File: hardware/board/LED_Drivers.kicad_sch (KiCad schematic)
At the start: 69 parts

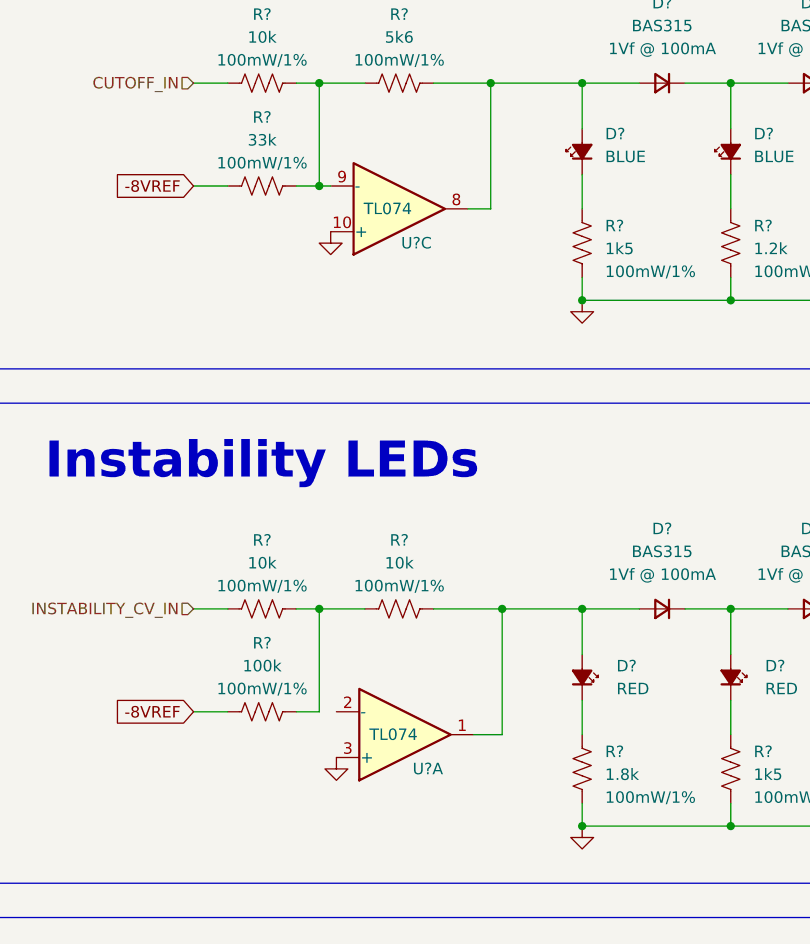
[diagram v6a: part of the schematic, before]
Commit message: First Draft of layout V2 (All components facing the same way)
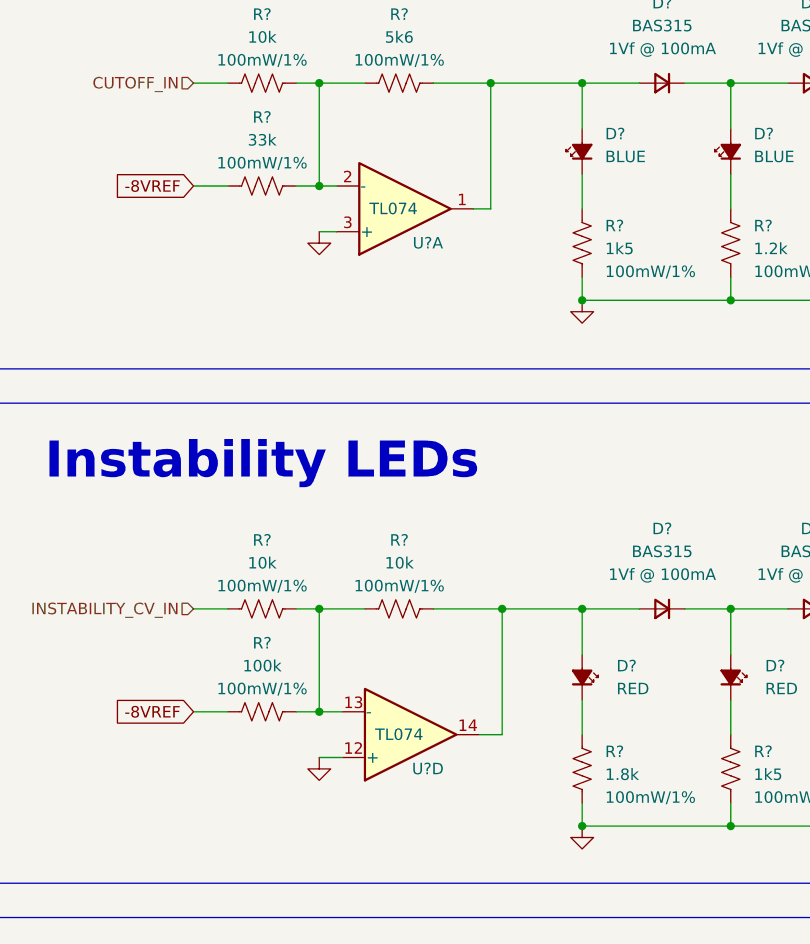
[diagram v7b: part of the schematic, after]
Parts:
- removed U?: TL074, Package_SO:TSSOP-14_4.4x5mm_P0.65mm, symbol winterbloom:TL074
- added U?: TL074, Package_SO:TSSOP-14_4.4x5mm_P0.65mm, symbol winterbloom:TL074
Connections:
- net GND: now also U?.12 (+)
- net at D?.2 (A), D?.2 (A), R?.1: now also U?.1
- net at R?.1, R?.1, R?.2: now also U?.2 (-)
- net at R?.1, R?.1, R?.2: now also U?.13 (-)
- net at D?.2 (A), D?.2 (A), R?.1: now also U?.14; no longer U?.1
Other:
- moved on the sheet: U?A
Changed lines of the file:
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@@
   (junction (at 208.28 119.38) (diameter 0) (color 0 0 0 0)
   )
+  (junction (at 55.88 64.77) (diameter 0) (color 0 0 0 0)
+  )
   (junction (at 205.74 53.34) (diameter 0) (color 0 0 0 0)
   )
@@
   (junction (at 85.09 77.47) (diameter 0) (color 0 0 0 0)
   )
+  (junction (at 55.88 123.19) (diameter 0) (color 0 0 0 0)
+  )
   (junction (at 55.88 167.64) (diameter 0) (color 0 0 0 0)
   )
-  (junction (at 55.88 64.77) (diameter 0) (color 0 0 0 0)
-  )
   (junction (at 224.79 153.67) (diameter 0) (color 0 0 0 0)
   )
@@
     (stroke (width 0) (type default))
   )
+  (wire (pts (xy 55.88 128.27) (xy 58.42 128.27))
+    (stroke (width 0) (type default))
+  )
   (wire (pts (xy 85.09 74.93) (xy 85.09 77.47))
     (stroke (width 0) (type default))
@@
     (stroke (width 0) (type default))
   )
+  (wire (pts (xy 73.025 67.31) (xy 74.93 67.31))
+    (stroke (width 0) (type default))
+  )
   (wire (pts (xy 173.99 64.77) (xy 176.53 64.77))
     (stroke (width 0) (type default))
@@
     (stroke (width 0) (type default))
   )
+  (wire (pts (xy 55.88 123.19) (xy 58.42 123.19))
+    (stroke (width 0) (type default))
+  )
   (wire (pts (xy 200.66 119.38) (xy 208.28 119.38))
     (stroke (width 0) (type default))
@@
     (stroke (width 0) (type default))
   )
-  (wire (pts (xy 57.15 64.77) (xy 55.88 64.77))
-    (stroke (width 0) (type default))
-  )
   (wire (pts (xy 85.09 167.64) (xy 85.09 172.72))
     (stroke (width 0) (type default))
@@
     (stroke (width 0) (type default))
   )
-  (wire (pts (xy 73.025 125.73) (xy 76.2 125.73))
-    (stroke (width 0) (type default))
-  )
   (wire (pts (xy 85.09 189.23) (xy 85.09 194.31))
     (stroke (width 0) (type default))
@@
     (stroke (width 0) (type default))
   )
+  (wire (pts (xy 73.66 125.73) (xy 76.2 125.73))
+    (stroke (width 0) (type default))
+  )
   (wire (pts (xy 205.74 53.34) (xy 205.74 58.42))
     (stroke (width 0) (type default))
@@
     (stroke (width 0) (type default))
   )
+  (wire (pts (xy 55.88 64.77) (xy 57.785 64.77))
+    (stroke (width 0) (type default))
+  )
   (wire (pts (xy 208.28 133.35) (xy 219.71 133.35))
     (stroke (width 0) (type default))
@@
     (stroke (width 0) (type default))
   )
+  (wire (pts (xy 55.88 69.85) (xy 57.785 69.85))
+    (stroke (width 0) (type default))
+  )
   (wire (pts (xy 224.79 119.38) (xy 228.6 119.38))
     (stroke (width 0) (type default))
@@
   )
   (wire (pts (xy 76.2 167.64) (xy 76.2 181.61))
-    (stroke (width 0) (type default))
-  )
-  (wire (pts (xy 72.39 67.31) (xy 74.93 67.31))
     (stroke (width 0) (type default))
   )
@@
     )
   )
-  (symbol (lib_id "winterbloom:TL074") (at 64.77 67.31 0) (mirror x) (unit 3)
-    (in_bom yes) (on_board yes) (dnp no)
-    (property "Reference" "U?" (at 66.675 71.12 0)
-      (effects (font (size 1.27 1.27)))
-    )
-    (property "Value" "TL074" (at 63.5 67.31 0)
-      (effects (font (size 1.27 1.27)))
-    )
-    (property "Footprint" "Package_SO:TSSOP-14_4.4x5mm_P0.65mm" (at 64.77 77.47 0)
-      (effects (font (size 1.27 1.27)) hide)
-    )
-    (property "Datasheet" "https://www.ti.com/lit/ds/symlink/tl071.pdf" (at 66.04 72.39 0)
-      (effects (font (size 1.27 1.27)) hide)
-    )
-    (property "MPN" "TL074CPW" (at 64.77 74.93 0)
+  (symbol (lib_id "winterbloom:TL074") (at 66.04 125.73 0) (mirror x) (unit 4)
+    (in_bom yes) (on_board yes) (dnp no)
+    (property "Reference" "U?" (at 67.945 129.54 0)
+      (effects (font (size 1.27 1.27)))
+    )
+    (property "Value" "TL074" (at 64.77 125.73 0)
+      (effects (font (size 1.27 1.27)))
+    )
+    (property "Footprint" "Package_SO:TSSOP-14_4.4x5mm_P0.65mm" (at 66.04 135.89 0)
+      (effects (font (size 1.27 1.27)) hide)
+    )
+    (property "Datasheet" "https://www.ti.com/lit/ds/symlink/tl071.pdf" (at 67.31 130.81 0)
+      (effects (font (size 1.27 1.27)) hide)
+    )
+    (property "MPN" "TL074CPW" (at 66.04 133.35 0)
       (effects (font (size 1.27 1.27)) hide)
     )
@@
     (pin "4")
     (instances
-      (project "VCA_0.3"
-        (path "/0739a502-7fa1-4e85-8cae-604fd21c9156"
-          (reference "U?") (unit 3)
-        )
-      )
       (project "mainboard"
         (path "/6e47ee4f-b36d-4cb2-9b20-31f755e664f7/00000000-0000-0000-0000-00005f0e55e2"
-          (reference "U?") (unit 3)
+          (reference "U?") (unit 4)
         )
         (path "/6e47ee4f-b36d-4cb2-9b20-31f755e664f7/00000000-0000-0000-0000-00005f016ad7"
-          (reference "U?") (unit 2)
-        )
-      )
-      (project "mainboard"
-        (path "/960bd036-bf0c-45ea-9f41-1321756e0e5a/2fb572ad-24ea-4cbe-ad52-b6fc76c2d017"
-          (reference "U?") (unit 3)
-        )
-        (path "/960bd036-bf0c-45ea-9f41-1321756e0e5a"
-          (reference "U?") (unit 3)
-        )
-        (path "/960bd036-bf0c-45ea-9f41-1321756e0e5a/48d891c0-35ba-4c8e-a930-c990a10298eb"
-          (reference "U4") (unit 3)
-        )
-        (path "/960bd036-bf0c-45ea-9f41-1321756e0e5a/e3d5295b-e037-4c01-a5ad-25ec0ca0bdb3"
-          (reference "U4") (unit 3)
-        )
-      )
-      (project "VCA"
-        (path "/de69ad6f-07bb-4f9c-962b-520f6532317d"
-          (reference "U?") (unit 3)
-        )
-        (path "/de69ad6f-07bb-4f9c-962b-520f6532317d/0f818280-e6cd-4382-a215-72bb59f50cc3"
-          (reference "U?") (unit 3)
+          (reference "U?") (unit 1)
+        )
+      )
+      (project "mainboard"
+        (path "/960bd036-bf0c-45ea-9f41-1321756e0e5a"
+          (reference "U?") (unit 4)
+        )
+        (path "/960bd036-bf0c-45ea-9f41-1321756e0e5a/3b1fa3f2-493c-449c-a2d6-10ea677680a0"
+          (reference "U?") (unit 4)
+        )
+        (path "/960bd036-bf0c-45ea-9f41-1321756e0e5a/48d891c0-35ba-4c8e-a930-c990a10298eb"
+          (reference "U4") (unit 4)
+        )
+        (path "/960bd036-bf0c-45ea-9f41-1321756e0e5a/e3d5295b-e037-4c01-a5ad-25ec0ca0bdb3"
+          (reference "U4") (unit 4)
         )
       )
@@
     )
   )
-  (symbol (lib_id "winterbloom:TL074") (at 65.405 125.73 0) (mirror x) (unit 1)
-    (in_bom yes) (on_board yes) (dnp no)
-    (property "Reference" "U?" (at 67.945 129.54 0)
-      (effects (font (size 1.27 1.27)))
-    )
-    (property "Value" "TL074" (at 64.135 125.73 0)
-      (effects (font (size 1.27 1.27)))
-    )
-    (property "Footprint" "Package_SO:TSSOP-14_4.4x5mm_P0.65mm" (at 65.405 135.89 0)
-      (effects (font (size 1.27 1.27)) hide)
-    )
-    (property "Datasheet" "https://www.ti.com/lit/ds/symlink/tl071.pdf" (at 66.675 130.81 0)
-      (effects (font (size 1.27 1.27)) hide)
-    )
-    (property "MPN" "TL074CPW" (at 65.405 133.35 0)
+  (symbol (lib_id "winterbloom:TL074") (at 65.405 67.31 0) (mirror x) (unit 1)
+    (in_bom yes) (on_board yes) (dnp no)
+    (property "Reference" "U?" (at 67.945 71.12 0)
+      (effects (font (size 1.27 1.27)))
+    )
+    (property "Value" "TL074" (at 64.135 67.31 0)
+      (effects (font (size 1.27 1.27)))
+    )
+    (property "Footprint" "Package_SO:TSSOP-14_4.4x5mm_P0.65mm" (at 65.405 77.47 0)
+      (effects (font (size 1.27 1.27)) hide)
+    )
+    (property "Datasheet" "https://www.ti.com/lit/ds/symlink/tl071.pdf" (at 66.675 72.39 0)
+      (effects (font (size 1.27 1.27)) hide)
+    )
+    (property "MPN" "TL074CPW" (at 65.405 74.93 0)
       (effects (font (size 1.27 1.27)) hide)
     )
@@
     )
   )
-  (symbol (lib_id "power:GND") (at 57.15 69.85 0) (unit 1)
+  (symbol (lib_id "power:GND") (at 55.88 69.85 0) (unit 1)
     (in_bom yes) (on_board yes) (dnp no) (fields_autoplaced)
-    (property "Reference" "#PWR?" (at 57.15 76.2 0)
-      (effects (font (size 1.27 1.27)) hide)
-    )
-    (property "Value" "GND" (at 57.277 74.2442 0)
-      (effects (font (size 1.27 1.27)) hide)
-    )
-    (property "Footprint" "" (at 57.15 69.85 0)
-      (effects (font (size 1.27 1.27)) hide)
-    )
-    (property "Datasheet" "" (at 57.15 69.85 0)
+    (property "Reference" "#PWR?" (at 55.88 76.2 0)
+      (effects (font (size 1.27 1.27)) hide)
+    )
+    (property "Value" "GND" (at 56.007 74.2442 0)
+      (effects (font (size 1.27 1.27)) hide)
+    )
+    (property "Footprint" "" (at 55.88 69.85 0)
+      (effects (font (size 1.27 1.27)) hide)
+    )
+    (property "Datasheet" "" (at 55.88 69.85 0)
       (effects (font (size 1.27 1.27)) hide)
     )
@@
     )
   )
-  (symbol (lib_id "power:GND") (at 57.785 128.27 0) (unit 1)
+  (symbol (lib_id "power:GND") (at 55.88 128.27 0) (unit 1)
     (in_bom yes) (on_board yes) (dnp no) (fields_autoplaced)
-    (property "Reference" "#PWR?" (at 57.785 134.62 0)
-      (effects (font (size 1.27 1.27)) hide)
-    )
-    (property "Value" "GND" (at 57.912 132.6642 0)
-      (effects (font (size 1.27 1.27)) hide)
-    )
-    (property "Footprint" "" (at 57.785 128.27 0)
-      (effects (font (size 1.27 1.27)) hide)
-    )
-    (property "Datasheet" "" (at 57.785 128.27 0)
-      (effects (font (size 1.27 1.27)) hide)
-    )
+    (property "Reference" "#PWR?" (at 55.88 134.62 0)
+      (effects (font (size 1.27 1.27)) hide)
+    )
+    (property "Value" "GND" (at 56.007 132.6642 0)
+      (effects (font (size 1.27 1.27)) hide)
+    )
+    (property "Footprint" "" (at 55.88 128.27 0)
+      (effects (font (size 1.27 1.27)) hide)
+    )
+    (property "Datasheet" "" (at 55.88 128.27 0)
+      (effects (font (size 1.27 1.27)) hide)
+    )

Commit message: Rough Draft of Routing Complete. Ugly but Passes DRC
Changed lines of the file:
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@@
     (fill (type none))
   )
-  (text "Red LED Indicates Self Oscillation" (at 87.63 153.67 0)
+  (text "Red LED Indicates\nSelf Oscillation" (at 120.65 154.94 0)
     (effects (font (size 2 2) (thickness 0.4) bold) (justify left bottom))
   )
